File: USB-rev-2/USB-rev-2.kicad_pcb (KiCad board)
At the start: 4 copper layers, 70 x 60 mm, 25 parts, among them J1 USBC-4-0-CX90MW9-24P1, U2 ESDA25L, U3 USB SWITCH 2CHANNEL TS3USB221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, U6 usb-polarity-TUSB321RWBR

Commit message: routing progress
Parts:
- moved J3 3.06 mm to (114.5, 74.7)
- moved J2 3.06 mm to (114.5, 79.2)
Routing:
- net 3V3B: track 3.13 -> 160.6 mm, vias 2 -> 3
- net 5V: track 0.00 -> 66.9 mm, vias 4 -> 40
- net RX2+: track 9.84 -> 13.1 mm
- net RX2-: track 9.84 -> 13.1 mm
- net D-: track 18.2 -> 21.0 mm
- net D+: track 22.3 -> 22.9 mm
- added copper zone on F.Cu, net GND
- added copper zone on F.Cu, net USBC POW
- removed copper zone on B.Cu, net 5V
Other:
- board size 70 x 60 mm -> 70.3 x 60 mm

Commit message: routing completeish need DRC
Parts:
- moved D2 7.93 mm to (128.4, 83.2)
- moved D1 0.40 mm to (118.2, 85.6)
- moved R1 0.32 mm to (103.5, 92.0)
- moved C6 0.14 mm to (105.8, 94.5)
- moved C7 0.14 mm to (107.3, 94.5)
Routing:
- net 3V3B: track 160.6 -> 17.5 mm, vias 3 -> 6
- net CC2-jumpered: track 0.00 -> 65.4 mm, vias 0 -> 2
- net CC1-jumpered: track 0.00 -> 61.7 mm, vias 0 -> 2
- net MUX POL: track 0.00 -> 37.5 mm, vias 0 -> 2
- net 5V: track 66.9 -> 100.0 mm
- net CC2: track 0.00 -> 31.2 mm
- net USB SWITCH: track 0.00 -> 20.5 mm, vias 0 -> 1
- net CC1: track 0.00 -> 19.7 mm, vias 0 -> 2
- net GND: track 51.7 -> 71.1 mm, vias 0 -> 71
- net Net-(MUX1-AMSEL): track 0.00 -> 5.88 mm, vias 0 -> 2
- net Net-(MUX1-EN): track 0.00 -> 5.67 mm
- net CHARGER D-: track 2.57 -> 6.67 mm
- net CHARGER D+: track 3.24 -> 6.63 mm
- net TX2+: track 12.6 -> 12.0 mm
- net TX2-: track 12.6 -> 12.0 mm
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- added copper zone on B.Cu, net 3V3B
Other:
- board text removed: "+"

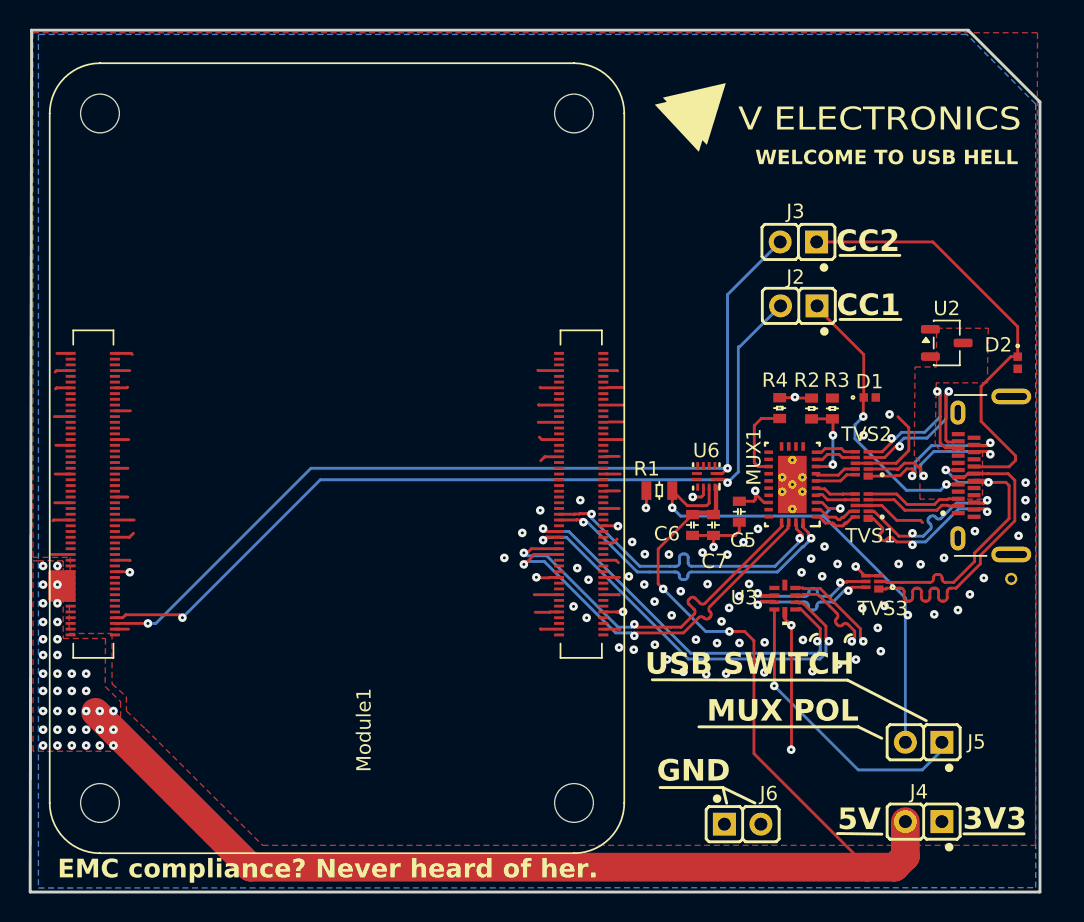
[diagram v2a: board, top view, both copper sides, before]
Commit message: fix stuff pointed out by DRC
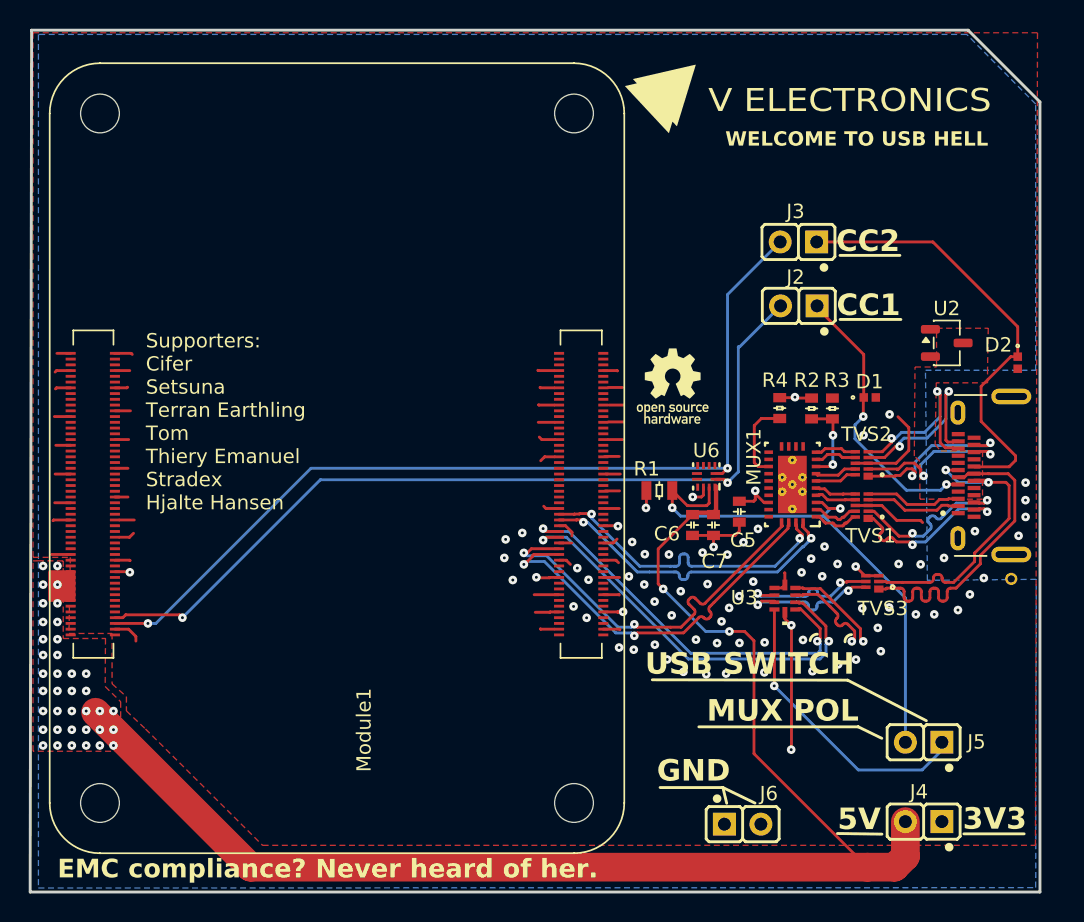
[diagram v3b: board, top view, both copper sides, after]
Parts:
- added G***: LOGO, LOGO, F.Cu at (104.4, 84.8)
- moved G*** 2.45 mm to (103.6, 64.8)
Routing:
- net GND: track 71.1 -> 78.1 mm
